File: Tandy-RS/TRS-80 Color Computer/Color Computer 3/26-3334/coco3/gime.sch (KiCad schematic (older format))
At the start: 9 parts, among them CN3 Conn_02x05_Odd_Even, IC11 74LS244, IC12 74LS244, IC13 74LS374, IC6 TCC1014, IC9 74LS138

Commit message: finished GIME section
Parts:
- removed CN3: Conn_02x05_Odd_Even, Connector_PinHeader_2.54mm:PinHeader_2x05_P2.54mm_Vertical, symbol Connector_Generic:Conn_02x05_Odd_Even
- removed IC11, UIC10: 74LS244, Package_DIP:DIP-20_W7.62mm_Socket, symbol 74xx:74LS244
- removed IC13: 74LS374, Package_DIP:DIP-20_W7.62mm_Socket, symbol 74xx:74LS374
- removed R61, R62: 4.7K, Resistor_THT:R_Axial_DIN0207_L6.3mm_D2.5mm_P10.16mm_Horizontal, symbol Device:R_Small_US
- added C10, C11: 39pF, Capacitor_THT:C_Disc_D4.7mm_W2.5mm_P5.00mm, symbol Device:C_Small
- added C12, C38, C39, C40, C41, C8: .1uF, Capacitor_THT:C_Disc_D4.7mm_W2.5mm_P5.00mm, symbol Device:C_Small
- added C60: 33pF, Capacitor_THT:C_Rect_L7.2mm_W3.0mm_P5.00mm_FKS2_FKP2_MKS2_MKP2, symbol Device:C_Small
- added C64: 150pF, Capacitor_THT:C_Rect_L7.2mm_W2.5mm_P5.00mm_FKS2_FKP2_MKS2_MKP2, symbol Device:C_Small
- added C9: 100uF 16V, Capacitor_THT:CP_Radial_D5.0mm_P2.00mm, symbol Device:CP_Small
- added FB5: Ferrite_Bead_Small, coco2:ferrite_bead, symbol Device:Ferrite_Bead_Small
- added IC10, IC11: 74LS244, Package_DIP:DIP-20_W7.62mm_Socket, symbol coco2:74LS244
- added IC13: 74LS374, Package_DIP:DIP-20_W7.62mm_Socket, symbol coco2:74LS374
- added IC15: 74LS04, Package_DIP:DIP-14_W7.62mm_Socket, symbol 74xx:74LS04
- added L1: 1.8uH, Inductor_THT:L_Axial_L9.5mm_D4.0mm_P12.70mm_Horizontal_Fastron_SMCC, symbol Device:L
- added R10, R9: 47, Resistor_THT:R_Axial_DIN0309_L9.0mm_D3.2mm_P12.70mm_Horizontal, symbol Device:R_Small_US
- added R11, R8: 4.7K, Resistor_THT:R_Axial_DIN0207_L6.3mm_D2.5mm_P10.16mm_Horizontal, symbol Device:R_Small_US
- added R63: 150, Resistor_THT:R_Axial_DIN0309_L9.0mm_D3.2mm_P12.70mm_Horizontal, symbol Device:R_Small_US
- added R65: 1M, Resistor_THT:R_Axial_DIN0207_L6.3mm_D2.5mm_P10.16mm_Horizontal, symbol Device:R_Small_US
- added TC1: 10pF-50pF, coco2:C_Rect_L7.2mm_W7.2mm_P5.00mm_FKS2_FKP2_MKS2_MKP2, symbol Device:C_Variable
- added X1: Crystal, coco2:XTAL_ECS-286.3-20-46X, symbol Device:Crystal
- IC12: symbol 74xx:74LS244 -> coco2:74LS244
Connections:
- net labels added: A0, A1, A10, A11, A12, A13, A14, A15, A2, A3, A4, A5, A6, A7, A8, A9, A[0..15], B, CVIDEO, D0, D0Q0, D0Q1, D0Q2, D0Q3, D0Q4, D0Q5, D0Q6, D0Q7, D0Q[0..7], D1, D1Q0, D1Q1, D1Q2, D1Q3, D1Q4, D1Q5, D1Q6, D1Q7, D1Q[0..7], D2, D3, D4, D5, D6, D7, D[0..7], ECLK, G, GNDS, HSYNC, IL1, PIA_~CS2, QCLK, R, RAMD0, RAMD1, RAMD2, RAMD3, RAMD4, RAMD5, RAMD6, RAMD7, RAMD[0..7], R~W, SERINT, VCC1, VSYNC, Z0, Z1, Z2, Z3, Z4, Z5, Z6, Z7, Z8, Z[0..8], ~CART, ~CAS, ~CTS, ~RAS, ~RESET, ~ROM, ~SCS, ~SLENB, ~WE0, ~WE1
- net labels removed: RGB_OUT_10
- wire segments 8 -> 252
- no-connect marks 0 -> 4
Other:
- moved on the sheet: IC6, IC9

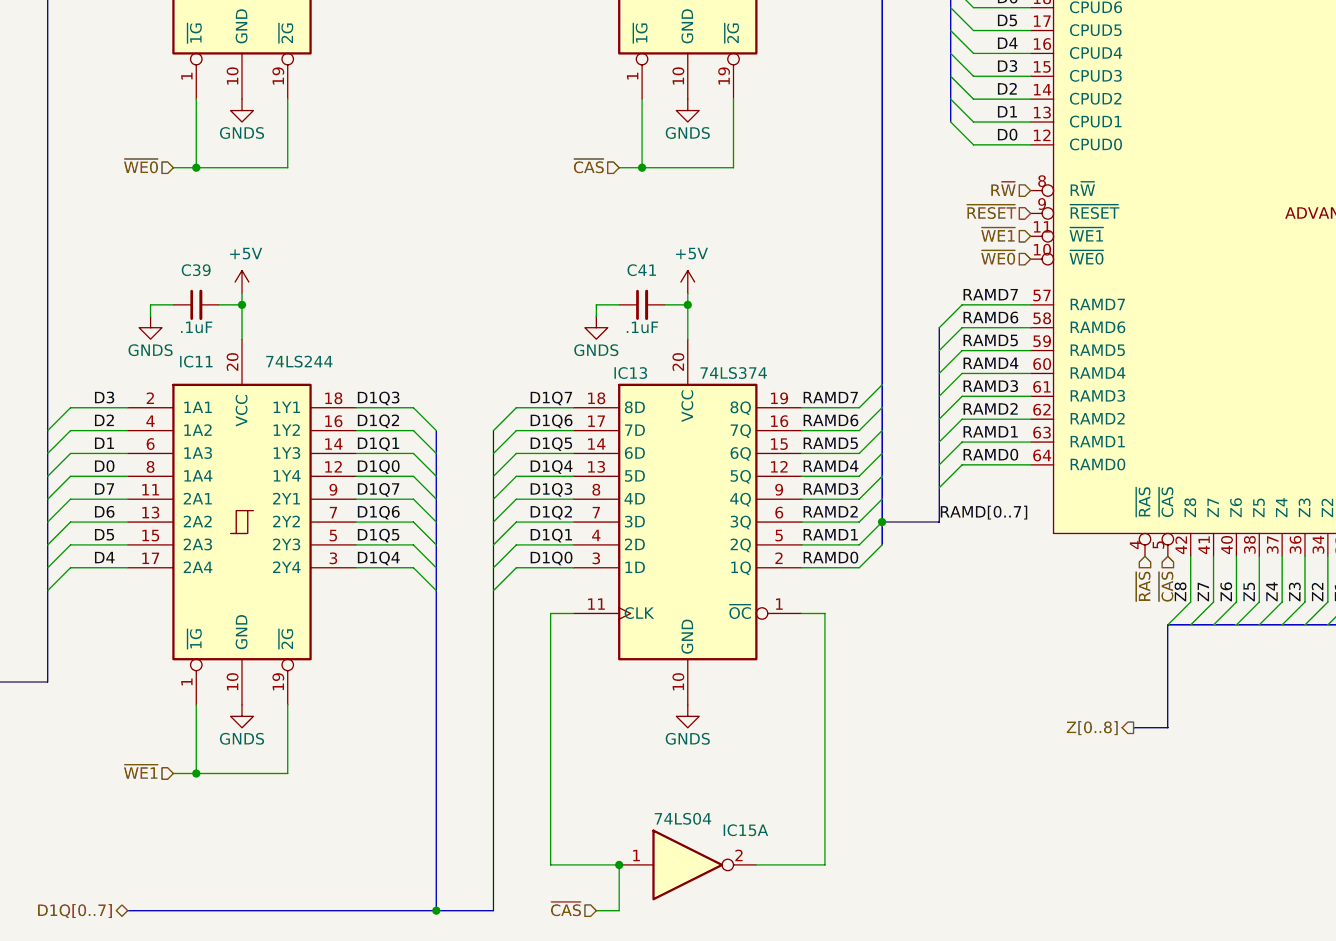
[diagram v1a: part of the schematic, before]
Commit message: cleaned up the peripherals sheet a little
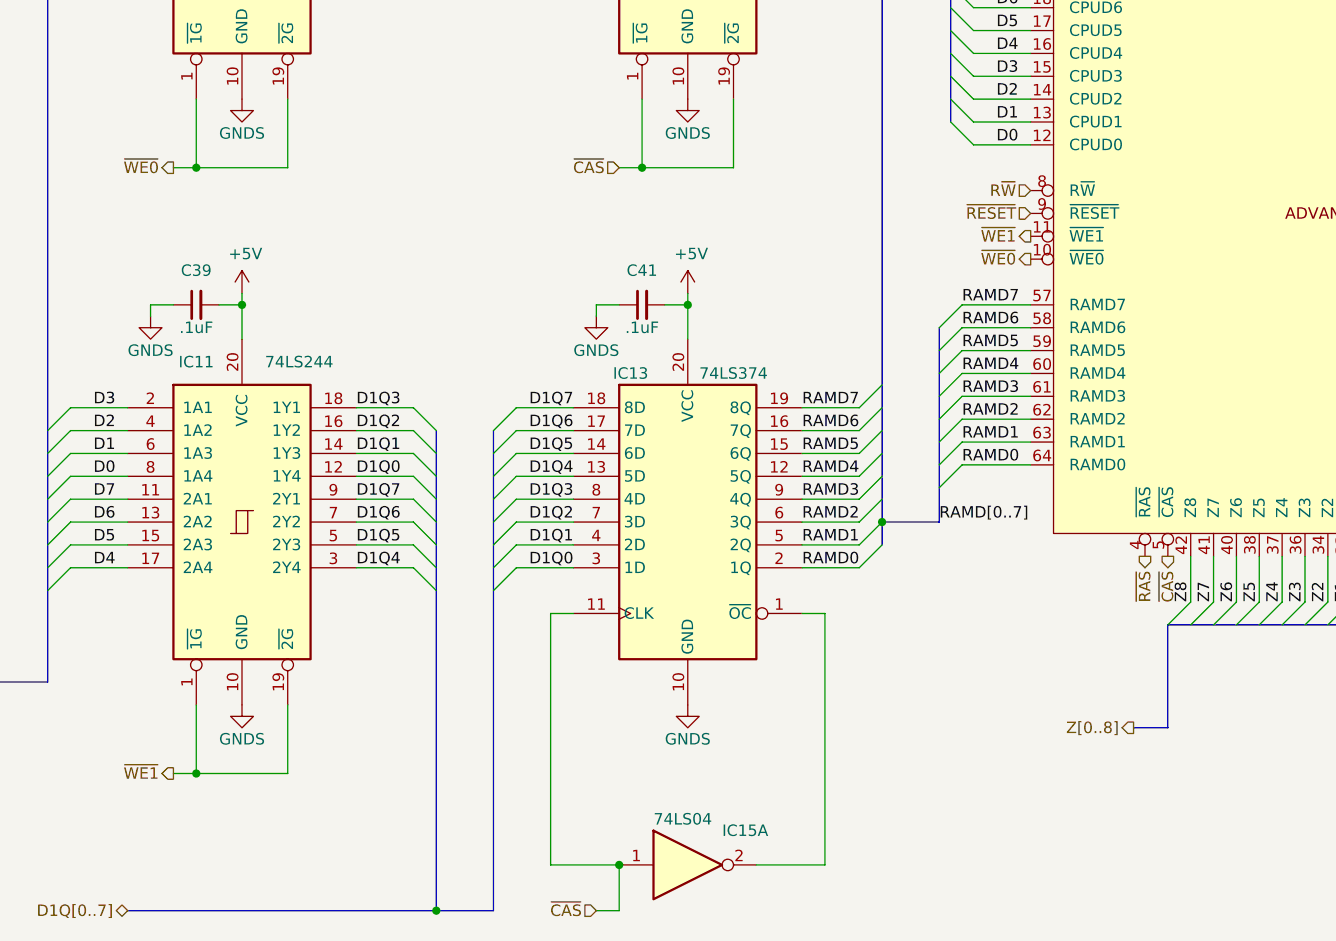
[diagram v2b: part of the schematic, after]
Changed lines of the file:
@@
 $Descr USLegal 14000 8500
 encoding utf-8
-Sheet 7 8
+Sheet 8 8
 Title "TRS-80 Color Computer 3 (26-3334)"
 Date "2021-07-12"
@@
 Text Label 5850 5250 0    50   ~ 0
 RAMD[0..7]
-Text HLabel 6250 4100 0    50   Input ~ 0
+Text HLabel 6250 4100 0    50   Output ~ 0
 ~WE0
-Text HLabel 6250 4000 0    50   Input ~ 0
+Text HLabel 6250 4000 0    50   Output ~ 0
 ~WE1
 Text HLabel 6250 3900 0    50   Input ~ 0
@@
 Wire Wire Line
 	3000 3700 3000 3400
-Text HLabel 2500 3700 0    50   Input ~ 0
+Text HLabel 2500 3700 0    50   Output ~ 0
 ~WE0
 Wire Wire Line
@@
 	2500 6350 2600 6350
 Connection ~ 2600 6350
-Text HLabel 2500 6350 0    50   Input ~ 0
+Text HLabel 2500 6350 0    50   Output ~ 0
 ~WE1
 Entry Wire Line
@@
 Wire Wire Line
 	4150 6750 4450 6750
-Text HLabel 6850 5400 3    50   Input ~ 0
+Text HLabel 6850 5400 3    50   Output ~ 0
 ~CAS
-Text HLabel 6750 5400 3    50   Input ~ 0
+Text HLabel 6750 5400 3    50   Output ~ 0
 ~RAS
 Text HLabel 4350 6950 0    50   Input ~ 0
@@
 AR Path="/603D560B/610B85A0" Ref="#PWR?"  Part="1"
 AR Path="/610B85A0" Ref="#PWR?"  Part="1"
-AR Path="/61257512/610B85A0" Ref="#PWR?"  Part="1"
+AR Path="/61257512/610B85A0" Ref="#PWR01083"  Part="1"
 AR Path="/612A4892/610B85A0" Ref="#PWR?"  Part="1"
-F 0 "#PWR?" H 12700 900 50  0001 C CNN
+F 0 "#PWR01083" H 12700 900 50  0001 C CNN
 F 1 "+5V" H 12715 1223 50  0000 C CNN
 F 2 "" H 12700 1050 50  0001 C CNN
@@
 AR Path="/603D345E/610B85A6" Ref="#PWR?"  Part="1"
 AR Path="/610B85A6" Ref="#PWR?"  Part="1"
-AR Path="/61257512/610B85A6" Ref="#PWR?"  Part="1"
-F 0 "#PWR?" H 12700 2000 50  0001 C CNN
+AR Path="/61257512/610B85A6" Ref="#PWR01084"  Part="1"
+F 0 "#PWR01084" H 12700 2000 50  0001 C CNN
 F 1 "GNDS" H 12700 2100 50  0000 C CNN
 F 2 "" H 12700 2250 50  0001 C CNN

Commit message: finished peripherals sheet
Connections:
- net ~VSYNC: now reaches IC15.13, IC6.55 (~VSYNC)
- net ~HSYNC: now reaches IC15.11, IC6.56 (~HSYNC)
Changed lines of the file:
@@
 	8850 5700 9700 5700
 Wire Wire Line
-	9700 5700 9700 6200
+	9700 5700 9700 6000
 Wire Wire Line
 	9700 6200 9800 6200
-Wire Wire Line
-	8700 5400 8700 5850
-Wire Wire Line
-	8700 5850 9550 5850
-Wire Wire Line
-	9550 5850 9550 6500
-Wire Wire Line
-	9550 6500 10150 6500
 $Comp
 L Device:R_Small_US R?
@@
 Wire Bus Line
 	1950 5950 1700 5950
+Text HLabel 9500 6000 0    50   Output ~ 0
+~VSYNC
+Wire Wire Line
+	8700 5400 8700 6500
+Wire Wire Line
+	8700 6500 9700 6500
+Wire Wire Line
+	9500 6000 9700 6000
+Connection ~ 9700 6000
+Wire Wire Line
+	9700 6000 9700 6200
+Text HLabel 9500 6300 0    50   Output ~ 0
+~HSYNC
+Wire Wire Line
+	9500 6300 9700 6300
+Wire Wire Line
+	9700 6300 9700 6500
 Wire Bus Line
 	3650 4850 3650 6950
@@
 Wire Bus Line
 	6100 2150 8050 2150
+Connection ~ 9700 6500
+Wire Wire Line
+	9700 6500 10150 6500
 $EndSCHEMATC

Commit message: added some more to the video sheet
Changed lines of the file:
@@
 	10250 4650 10050 4650
 Connection ~ 10500 4350
-Text Label 9600 4400 0    50   ~ 0
-VCC1
-Wire Wire Line
-	9600 4400 9600 4650
 Connection ~ 9600 4650
 Wire Wire Line
 	9600 4650 9450 4650
-Text Label 12500 5700 0    50   ~ 0
-VCC1
 $Comp
 L power:GNDS #PWR?
@@
 Wire Wire Line
 	12600 6000 12500 6000
-Wire Wire Line
-	12500 6000 12500 5700
 Wire Wire Line
 	12600 6350 12500 6350
@@
 Wire Wire Line
 	9700 6500 10150 6500
+Text GLabel 9700 4300 2    50   Input ~ 0
+VCC1
+Wire Wire Line
+	9700 4300 9600 4300
+Wire Wire Line
+	9600 4300 9600 4650
+Text GLabel 12600 5450 2    50   Input ~ 0
+VCC1
+Wire Wire Line
+	12600 5450 12500 5450
+Wire Wire Line
+	12500 5450 12500 6000
 Wire Bus Line
 	3650 4850 3650 6950

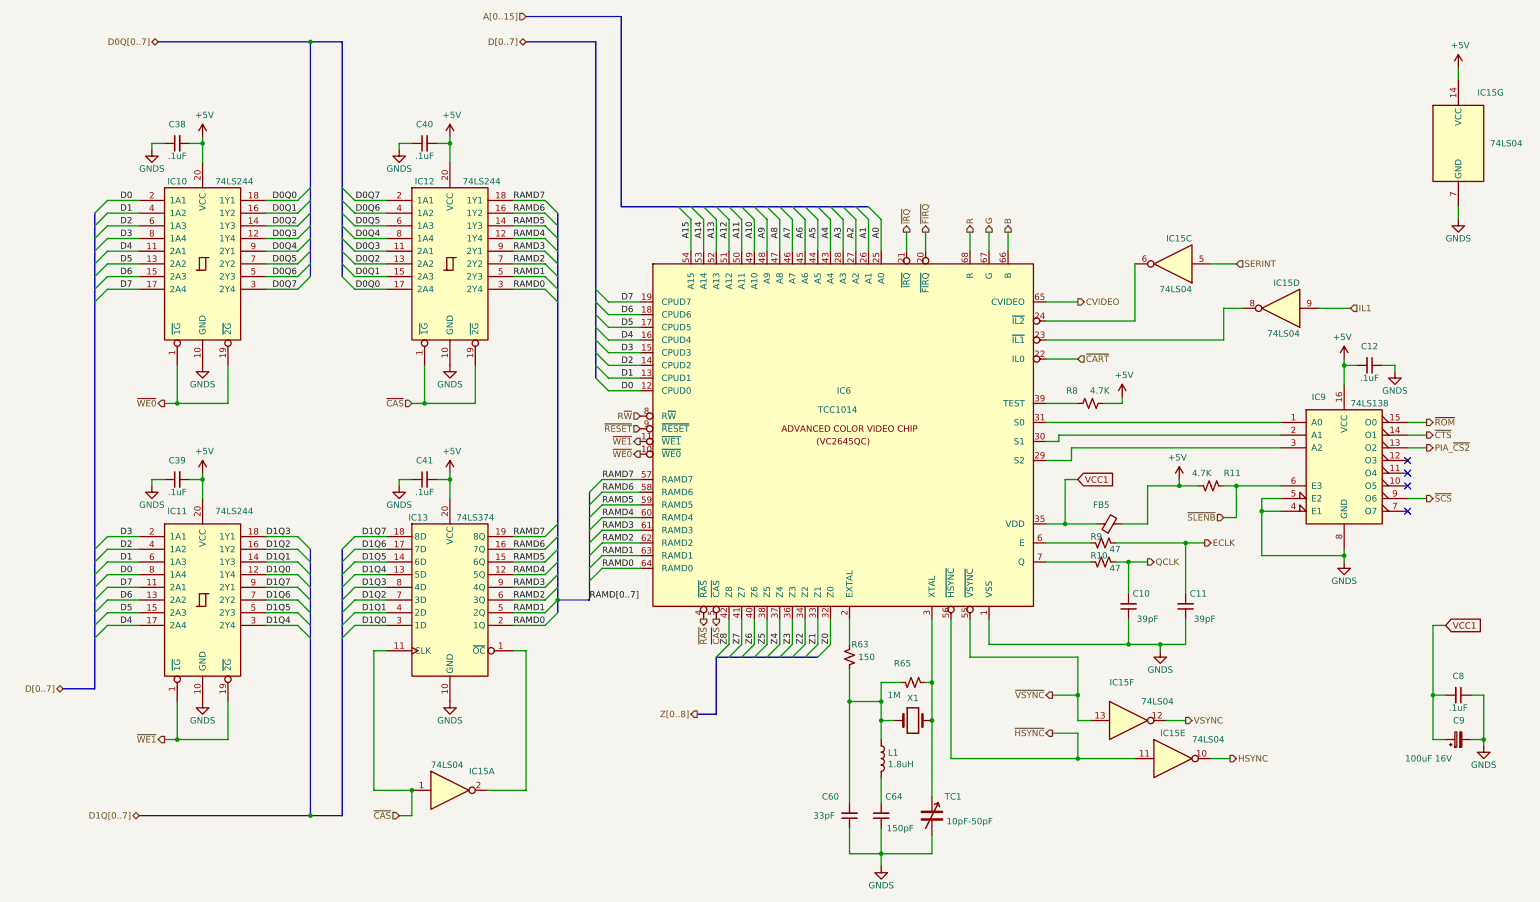
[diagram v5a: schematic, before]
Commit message: finished video sheet
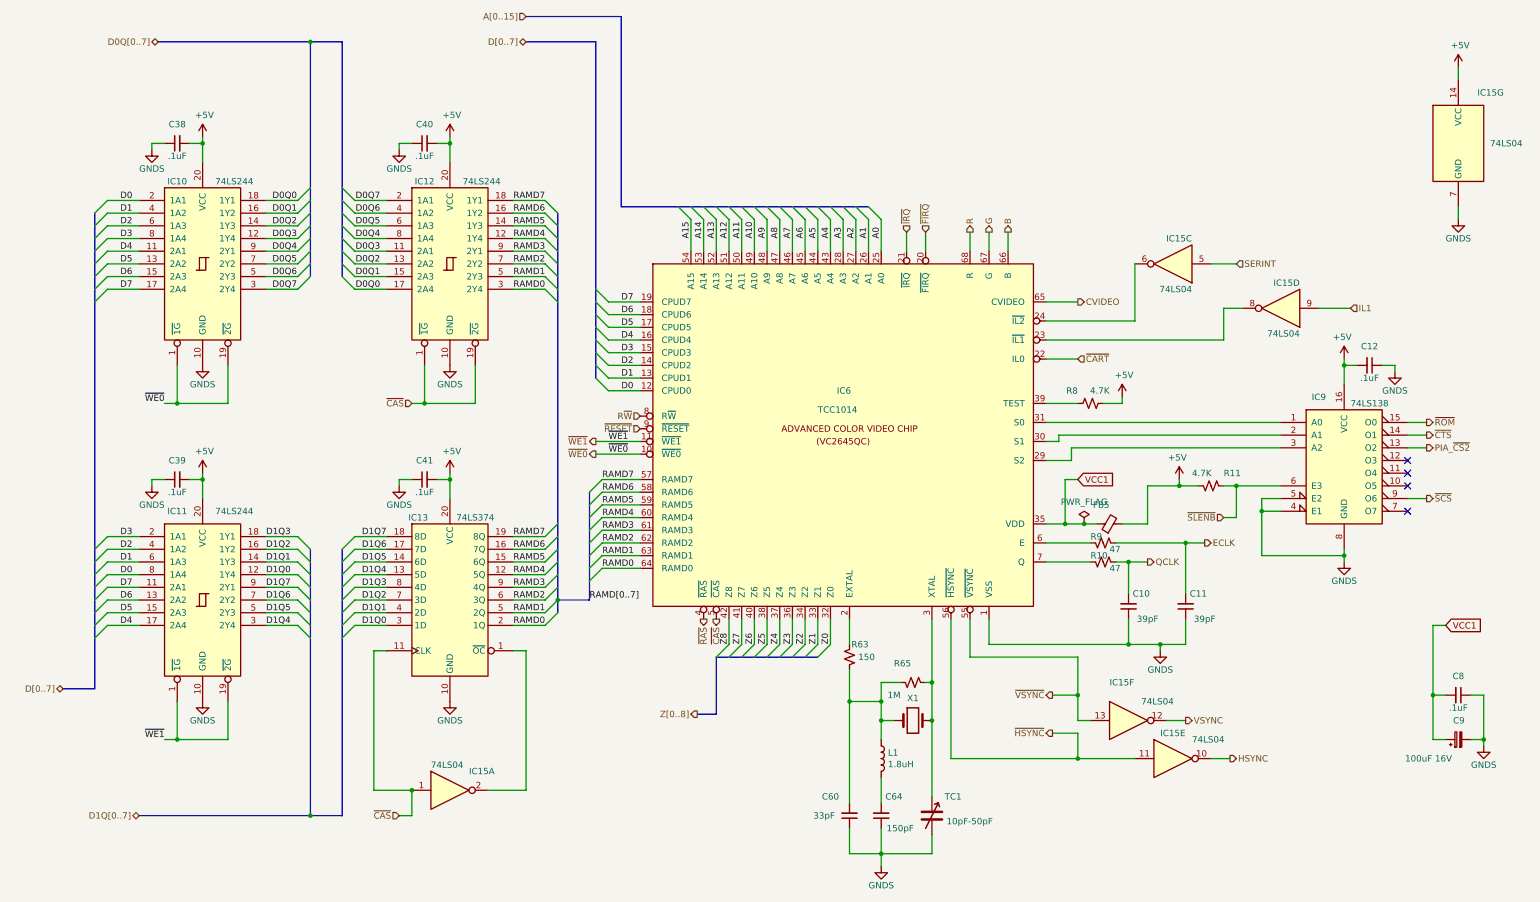
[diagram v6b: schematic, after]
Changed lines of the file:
@@
 	1    0    0    -1
 $EndComp
-Text HLabel 8350 2350 1    50   Output ~ 0
+Text HLabel 8350 2350 1    50   Input ~ 0
 ~IRQ
-Text HLabel 8500 2350 1    50   Output ~ 0
+Text HLabel 8500 2350 1    50   Input ~ 0
 ~FIRQ
 Wire Wire Line
@@
 Text Label 5850 5250 0    50   ~ 0
 RAMD[0..7]
-Text HLabel 6250 4100 0    50   Output ~ 0
+Text HLabel 5900 4100 0    50   Output ~ 0
 ~WE0
-Text HLabel 6250 4000 0    50   Output ~ 0
-~WE1
 Text HLabel 6250 3900 0    50   Input ~ 0
 ~RESET
@@
 Wire Wire Line
 	3000 3700 3000 3400
-Text HLabel 2500 3700 0    50   Output ~ 0
-~WE0
 Wire Wire Line
 	2500 3700 2600 3700
@@
 	2500 6350 2600 6350
 Connection ~ 2600 6350
-Text HLabel 2500 6350 0    50   Output ~ 0
-~WE1
 Entry Wire Line
 	3650 2100 3550 2200
@@
 $EndComp
 Wire Wire Line
-	9850 4650 9600 4650
+	9850 4650 9750 4650
 Wire Wire Line
 	10500 4350 10250 4350
@@
 Wire Wire Line
 	12500 5450 12500 6000
+Wire Wire Line
+	5900 4000 6250 4000
+Wire Wire Line
+	5900 4100 6250 4100
+Text Label 2500 3700 2    50   ~ 0
+~WE0
+Text Label 2500 6350 2    50   ~ 0
+~WE1
+$Comp
+L power:PWR_FLAG #FLG0101
+U 1 1 612850E1
+P 9750 4650
+F 0 "#FLG0101" H 9750 4725 50  0001 C CNN
+F 1 "PWR_FLAG" H 9750 4823 50  0000 C CNN
+F 2 "" H 9750 4650 50  0001 C CNN
+F 3 "~" H 9750 4650 50  0001 C CNN
+	1    9750 4650
+	1    0    0    -1
+$EndComp
+Connection ~ 9750 4650
+Wire Wire Line
+	9750 4650 9600 4650
+Text Label 6000 4100 0    50   ~ 0
+~WE0
+Text Label 6000 4000 0    50   ~ 0
+~WE1
+Wire Bus Line
+	1950 2200 1950 5950
+Wire Bus Line
+	6100 2150 8050 2150
+Wire Bus Line
+	5900 850  5900 3500
+Wire Bus Line
+	6850 5700 7650 5700
+Wire Bus Line
+	3900 4850 3900 6950
 Wire Bus Line
 	3650 4850 3650 6950
 Wire Bus Line
-	3900 4850 3900 6950
-Wire Bus Line
-	5900 850  5900 3500
-Wire Bus Line
-	6850 5700 7650 5700
-Wire Bus Line
 	3900 850  3900 2700
 Wire Bus Line
@@
 Wire Bus Line
 	5600 2200 5600 5250
-Wire Bus Line
-	1950 2200 1950 5950
-Wire Bus Line
-	6100 2150 8050 2150
+Text HLabel 5900 4000 0    50   Output ~ 0
+~WE1
 $EndSCHEMATC
